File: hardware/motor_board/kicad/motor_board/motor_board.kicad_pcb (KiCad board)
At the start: 6 copper layers, 85 x 35 mm, 236 parts, among them J1 BOOMELE_1.27-2x10P, J2 WAFER-SH1.0-6PWB, J3 WAFER-SH1.0-6PWB, J4 S5B-XH-A, Q1 HYG015N04LS1C2, Q2 HYG015N04LS1C2, Q3 HYG015N04LS1C2, Q4 HYG015N04LS1C2, Q5 HYG015N04LS1C2, Q6 HYG015N04LS1C2, Q7 HYG015N04LS1C2, Q8 HYG015N04LS1C2, U1 STM32G474RET6, U10 SN74LVC3G17DCUR, U11 TPS22945DCKR, U12 TPS22945DCKR, U13 LM74502DDFR, U14 74LVC1G17SE-7, U2 DRV8323RHRGZR, U3 DRV8316CRRGFR, U4 DRV8316CRRGFR, U5 AP2112K-3.3TRG1, U6 SN74LVC08APWR, U7 INA239AIDGSR, U8 BQ76907RGRR, U9 SN74LVC3G17DCUR

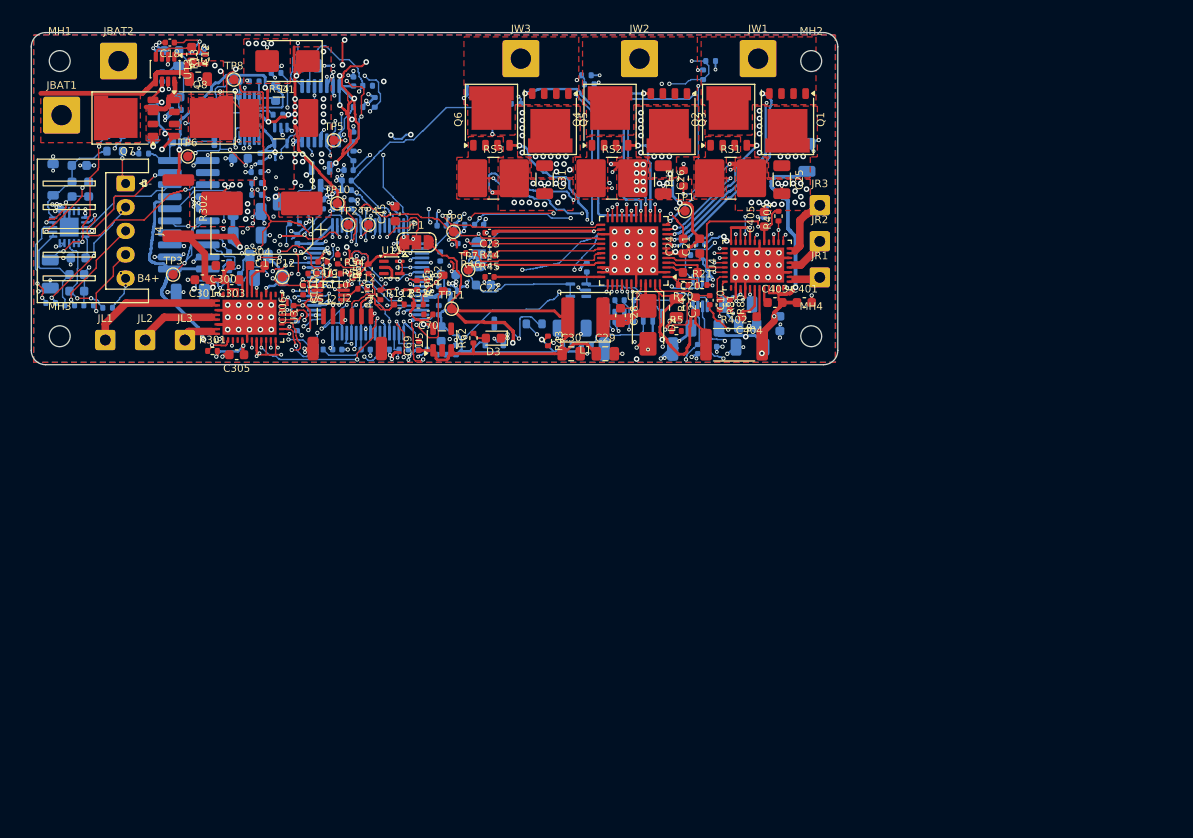
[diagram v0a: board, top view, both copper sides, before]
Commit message: v2: fresh 4-layer board built from the schematic (build_board.py): JLC041611-1080 stack-up, 85x35 outline, MH at the corners, all other parts staged off-board; design rules and custom DRC from JLC's 4-layer capabilities (with margin); 3D models applied. DRC 0, parity 0, 499 unrouted
Co-Authored-By: Claude Opus 5.5 (1M context) <noreply@anthropic.com>
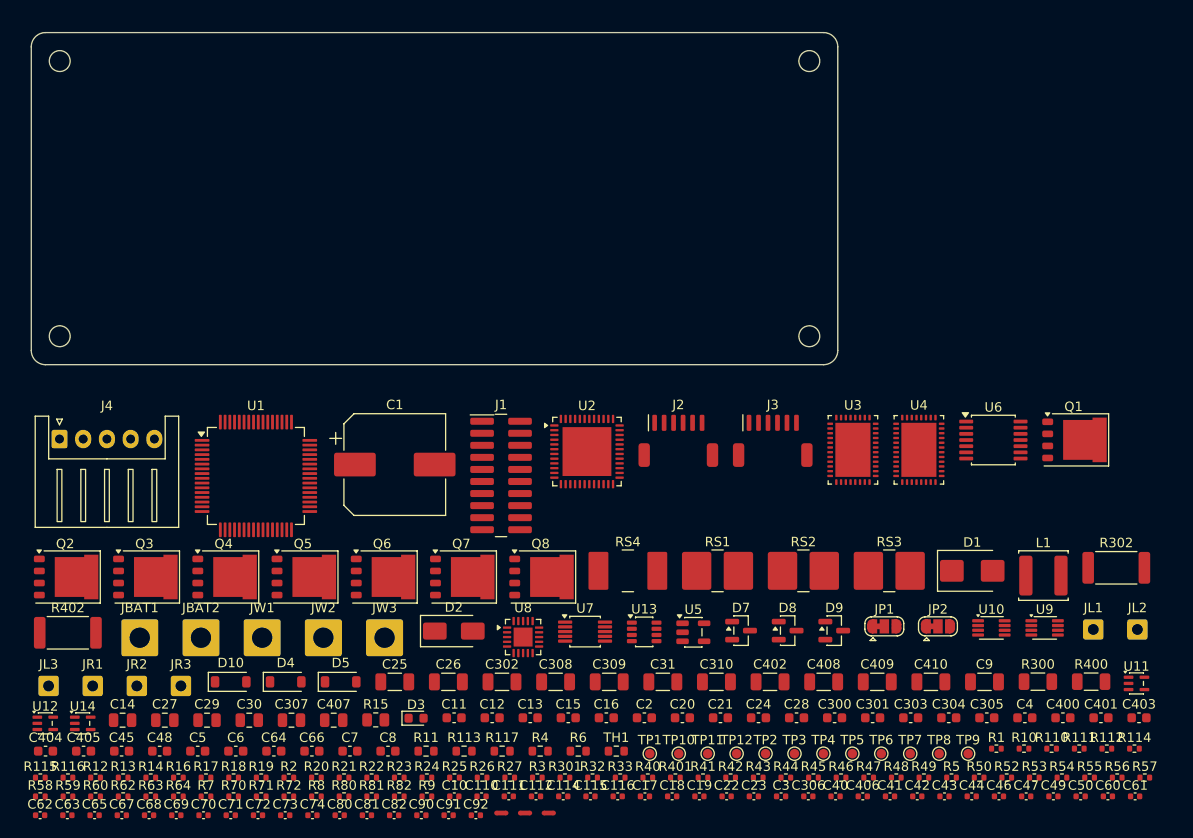
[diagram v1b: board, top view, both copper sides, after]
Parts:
- C11, C114, C115, C116, C13, C15, C16, C17, C19, C2, C3, C302, C307, C308, C309, C310, C4, C40, C400, C402, C406, C407, C408, C409, C41, C410, C42, C43, C44, C46, C48, C49, C5, C50, C6, C60, C61, C62, C63, C64, C65, C66, C67, C68, C7, C71, C73, C74, C8, C80, C81, C82, C9, C90, C91, D10, D4, D5, D7, D8, D9, J1, J3, JP2, R1, R10, R11, R114, R115, R116, R117, R12, R14, R15, R16, R17, R18, R19, R2, R22, R23, R24, R25, R26, R27, R3, R300, R32, R33, R40, R400, R41, R42, R47, R48, R49, R50, R53, R57, R58, R59, R6, R60, R63, R64, R7, R70, R71, R72, R8, R9, U1, U10, U12, U14, U6, U7, U8: moved to F.Cu
- moved C4 114.8 mm to (204.7, 142.2), turned to 0 degrees
- moved R1 112.9 mm to (201.7, 145.5), turned to 0 degrees
- moved JL2 108.9 mm to (216.6, 132.9)
- moved JL1 108.5 mm to (211.9, 132.9)
- moved C9 107.4 mm to (200.5, 138.4), turned to 0 degrees
- moved R10 107.2 mm to (204.6, 145.5), turned to 0 degrees
- moved R302 105.9 mm to (214.3, 126.4), turned to 0 degrees
- moved TP8 102.8 mm to (195.7, 146.0)
- moved R50 98.6 mm to (199.9, 148.5), turned to 0 degrees
- moved R56 97.3 mm to (214.4, 148.5), turned to 0 degrees
- moved TP6 96.5 mm to (189.6, 146.0)
- moved C18 95.5 mm to (167.5, 150.5), turned to 0 degrees
- moved C3 93.6 mm to (179.0, 150.5), turned to 0 degrees
- moved R49 93.6 mm to (194.1, 148.5)
- moved C47 93.1 mm to (204.9, 150.5), turned to 0 degrees
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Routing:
- net +3V3: track 349.5 -> 0.00 mm, vias 46 -> 0
- net GND: track 215.4 -> 0.00 mm, vias 269 -> 0
- net DRV_OFF: track 129.5 -> 0.00 mm, vias 5 -> 0
- net +5V: track 125.7 -> 0.00 mm, vias 2 -> 0
- net VBAT: track 116.9 -> 0.00 mm, vias 58 -> 0
- net SPI_SCK: track 101.7 -> 0.00 mm, vias 6 -> 0
- net W_EN: track 91.9 -> 0.00 mm, vias 7 -> 0
- net SPI_MISO: track 85.3 -> 0.00 mm, vias 6 -> 0
- net SPI_MOSI: track 79.7 -> 0.00 mm, vias 5 -> 0
- net W_VA: track 73.6 -> 0.00 mm, vias 7 -> 0
- net W_NTC: track 72.8 -> 0.00 mm, vias 7 -> 0
- net W_INLB_M: track 69.7 -> 0.00 mm, vias 7 -> 0
- net R_nFAULT: track 67.9 -> 0.00 mm, vias 2 -> 0
- net W_SOC: track 66.6 -> 0.00 mm, vias 10 -> 0
- net W_nFAULT: track 66.3 -> 0.00 mm, vias 8 -> 0
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- removed copper zone on In3.Cu, net +3V3
- removed copper zone on F.Cu, net /power/BAT_IN
- removed copper zone on F.Cu, net /power/PSW_S
- removed copper zone on F.Cu, net /power/VBAT_SW
- removed copper zone on F.Cu, net /weapon/W_A
- removed copper zone on F.Cu, net /weapon/W_B
- removed copper zone on F.Cu, net /weapon/W_C
- removed copper zone on F.Cu, net /weapon/W_SLA
- removed copper zone on F.Cu, net /weapon/W_SLB
- removed copper zone on F.Cu, net /weapon/W_SLC
- removed copper zone on B.Cu, net GND
- removed copper zone on F.Cu, net GND
- removed copper zone on In1.Cu, net GND
- removed copper zone on In4.Cu, net GND
- removed copper zone on F.Cu, net VBAT
- removed copper zone on In2.Cu, net VBAT
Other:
- copper layers 6 -> 4
- board text removed: "B-"
- board text removed: "B4+"
- board text removed: "BAT+"
- board text removed: "BAT-"
- board text removed: "FRONT (drum)"
- board text removed: "LA"
- board text removed: "LB"
- board text removed: "LC"
- board text removed: "MOTOR BOARD rev L"
- board text removed: "RA"
- board text removed: "RB"
- board text removed: "RC"
- board text removed: "T"
- board text removed: "VS J2"
- board text removed: "VS J3"
- board text removed: "WA"
- board text removed: "WB"
- board text removed: "WC"

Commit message: v2 package swaps (rev L2), after adversarial review: U6 WQFN-14 (EP to GND), D2 PMEG4030ER, L1 ZEMS404030 4.1 mm, J4 vertical XH, J2/J3 genuine JST vertical SH, R300/R400 0603 anti-surge, R15/C14/D10 one size down; drive VM bulk 2 x 10 uF X7R 1210 per drive (C309/C310/C409/C410 removed, user OK) - the 1206 X5R kept only ~2.3 uF at 16.8 V
sim_hotplug.py models MLCC DC bias (worst bounce 2.14 V/us at 0 C, 2.62 at -40 C); library check 0 errors, mutation test all caught; schematic regenerated, nets 176/176; v2 board rebuilt: DRC 0, parity 0; WQFN-14 3D model generated; DESIGN/calcs/BOM/FAB/CHANGES updated (CPL rotation fix for J2/J3/J4)

Co-Authored-By: Claude Opus 5.5 (1M context) <noreply@anthropic.com>
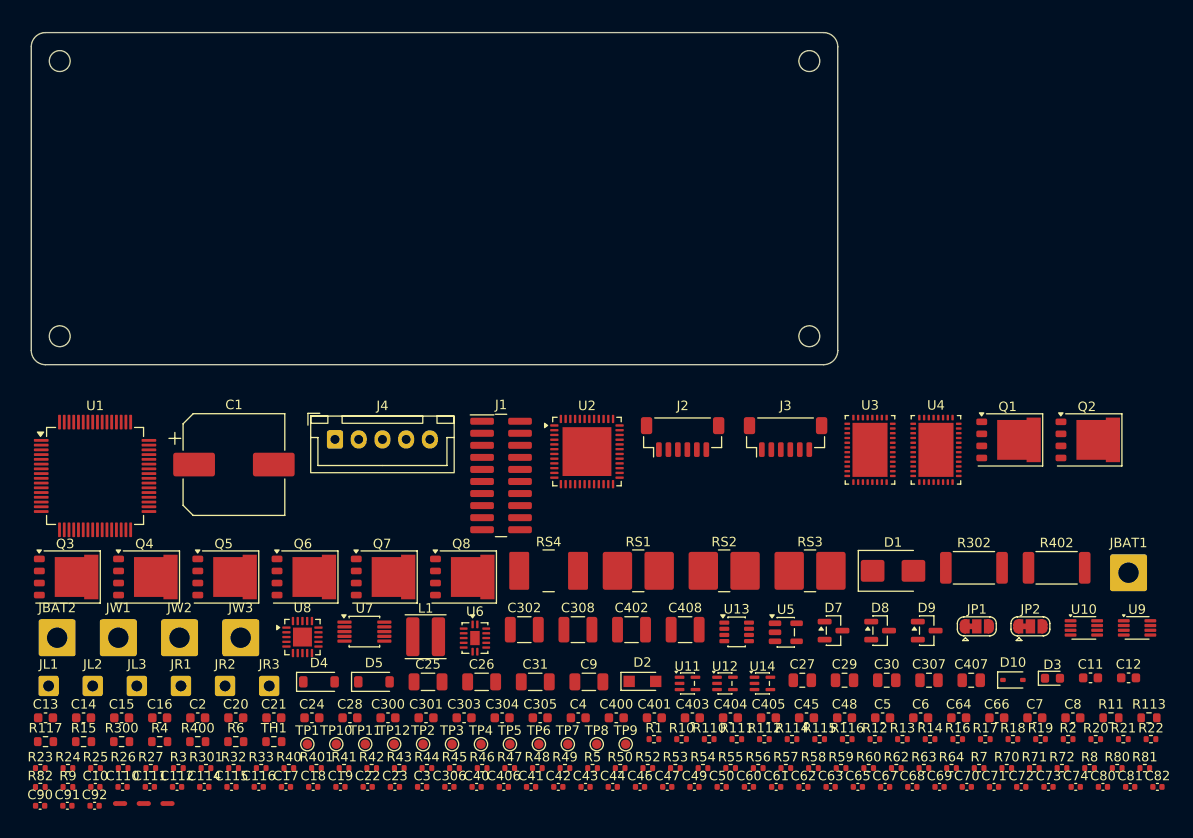
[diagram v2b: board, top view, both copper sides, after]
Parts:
- removed C309, C310, C409, C410: 10uF 50V, Capacitor_SMD:C_1206_3216Metric
- C14: footprint Capacitor_SMD:C_0805_2012Metric -> Capacitor_SMD:C_0603_1608Metric
- C302, C308, C402, C408: value 10uF 50V -> 10uF 50V X7R 1210; footprint Capacitor_SMD:C_1206_3216Metric -> Capacitor_SMD:C_1210_3225Metric
- D10: value 1N4148W -> 1N4148WS; footprint Diode_SMD:D_SOD-123 -> Diode_SMD:D_SOD-323
- D2: value SS34 -> PMEG4030ER; footprint Diode_SMD:D_SMA -> Diode_SMD:Nexperia_CFP3_SOD-123W
- J2, J3: value WAFER-SH1.0-6PWB -> BM06B-SRSS-TB; footprint motor_board:SH1.0-6P_RA_XUNPU_WAFER-SH1.0-6PWB -> Connector_JST:JST_SH_BM06B-SRSS-TB_1x06-1MP_P1.00mm_Vertical
- J4: value S5B-XH-A -> B5B-XH-A; footprint Connector_JST:JST_XH_S5B-XH-A_1x05_P2.50mm_Horizontal -> Connector_JST:JST_XH_B5B-XH-A_1x05_P2.50mm_Vertical
- L1: value FNR5040S220MT -> ZEMS404030-220M; footprint Inductor_SMD:L_Changjiang_FNR5040S -> Inductor_SMD:L_Changjiang_FTC404030S
- R15: value 6.8k 0805 -> 6.8k 0603; footprint Resistor_SMD:R_0805_2012Metric -> Resistor_SMD:R_0603_1608Metric
- R300, R400: value 22R 1206 -> 22R 0603 anti-surge; footprint Resistor_SMD:R_1206_3216Metric -> Resistor_SMD:R_0603_1608Metric
- U6: value SN74LVC08APWR -> SN74LVC08ABQAR; footprint Package_SO:TSSOP-14_4.4x5mm_P0.65mm -> Package_DFN_QFN:DHWQFN-14-1EP_2.5x3mm_P0.5mm_EP1x1.5mm
- moved JL1 110.3 mm to (101.8, 138.9)
- moved JL2 110.3 mm to (106.5, 138.9)
- moved Q2 108.6 mm to (211.2, 112.9)
- moved R402 104.4 mm to (208.1, 126.4)
- moved JBAT1 104.4 mm to (215.6, 126.9)
- moved R300 96.8 mm to (109.5, 144.7)
- moved R400 94.4 mm to (117.5, 144.7)
- moved D10 82.4 mm to (203.5, 138.2)
- moved R17 82.2 mm to (200.5, 144.5)
- moved R115 82.2 mm to (183.1, 144.5)
- moved R116 82.2 mm to (186.0, 144.5)
- moved R19 82.2 mm to (206.4, 144.5)
- moved R2 82.2 mm to (209.3, 144.5)
- moved R12 82.2 mm to (188.9, 144.5)
- moved R13 82.2 mm to (191.8, 144.5)
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
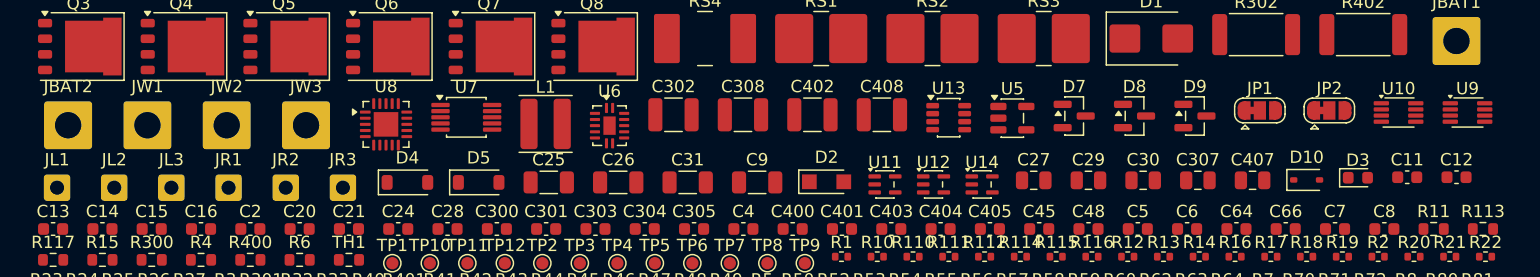
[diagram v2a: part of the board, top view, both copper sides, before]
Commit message: C25/C26/C31 -> 10 uF 50 V X7R 1210 (C77102, user OK): VDS-only fault kick at the DRV8316 VM 7.7 -> 4.3 V/us, bus peak ~30 -> ~22 V; hot-plug worst 1.86 V/us (0 C), 2.14 (-40 C), re-close 1.77; schematic regenerated (nets 176/176), board rebuilt (DRC 0, parity 0); DESIGN/calcs/BOM/CHANGES updated
Co-Authored-By: Claude Opus 5.5 (1M context) <noreply@anthropic.com>
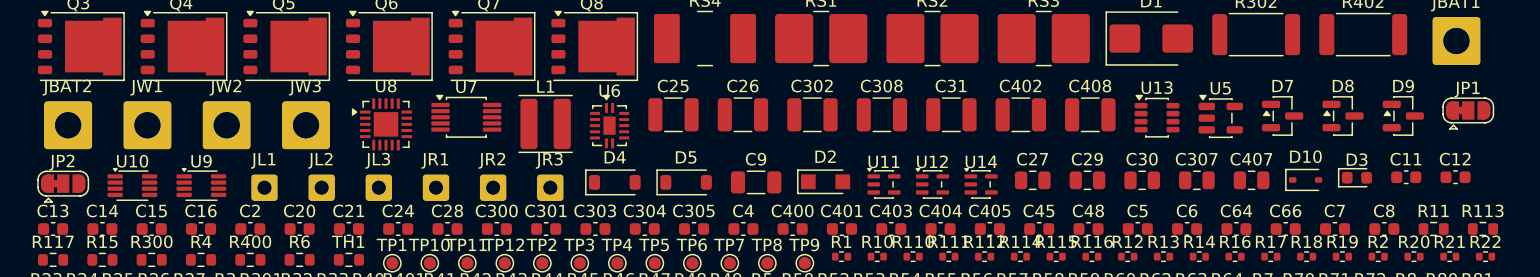
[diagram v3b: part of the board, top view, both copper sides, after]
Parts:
- C25, C26, C31: value 10uF 50V -> 10uF 50V X7R 1210; footprint Capacitor_SMD:C_1206_3216Metric -> Capacitor_SMD:C_1210_3225Metric
- moved JP2 103.1 mm to (102.3, 138.5)
- moved U10 103.1 mm to (108.0, 138.7)
- moved U9 103.1 mm to (113.6, 138.7)
- moved C31 22.1 mm to (174.6, 132.9)
- moved D8 17.0 mm to (206.4, 133.0)
- moved JP1 17.0 mm to (216.6, 132.6)
- moved U5 17.0 mm to (196.5, 133.2)
- moved C402 17.0 mm to (180.2, 132.9)
- moved C408 17.0 mm to (185.9, 132.9)
- moved D7 16.9 mm to (201.5, 133.0)
- moved D9 16.9 mm to (211.3, 133.0)
- moved U13 16.9 mm to (191.3, 133.2)
- moved D4 16.9 mm to (147.2, 138.4)
- moved D5 16.9 mm to (153.0, 138.4)
- moved JL2 16.9 mm to (123.3, 138.9)
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
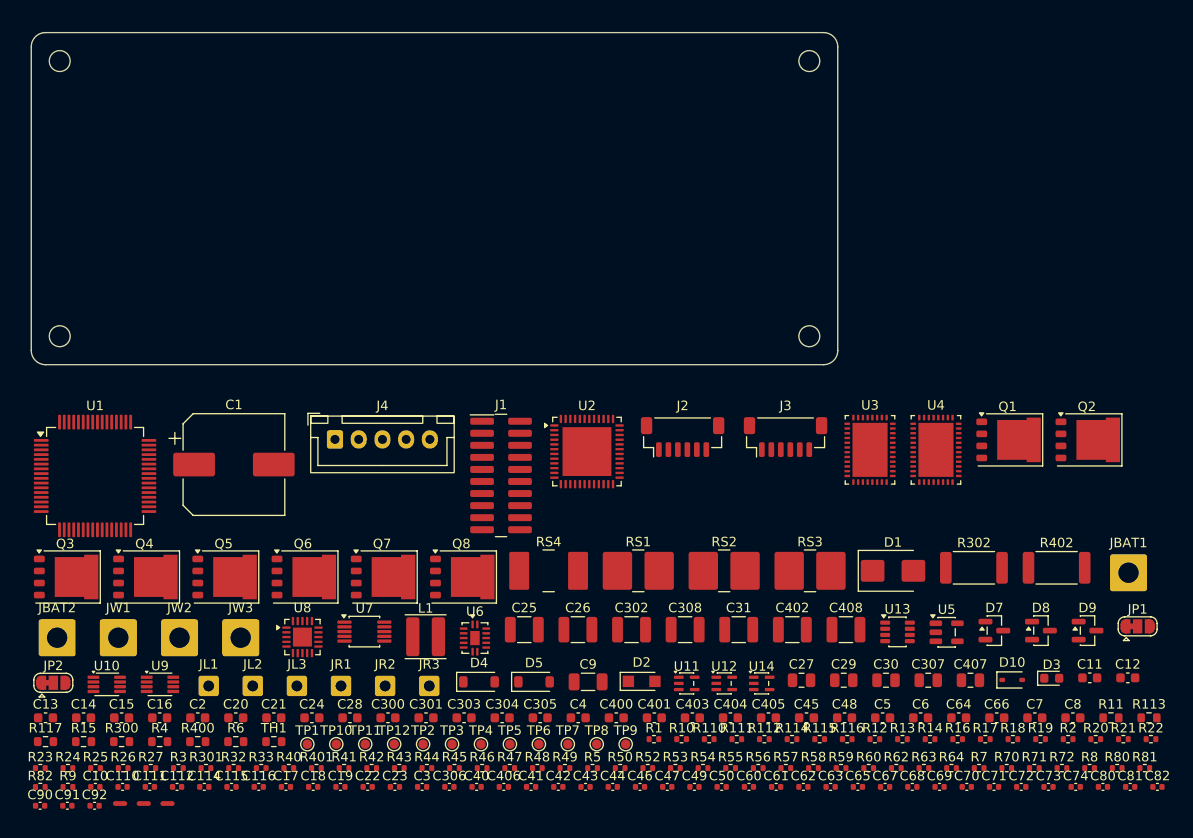
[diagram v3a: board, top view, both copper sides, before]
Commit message: v2 P1 placement: kicad/v2/place.py (attempt-1 engine + block regions) and spec.py (explicit key parts per the approved floorplan, the rest anchored automatically to the IC pin/net they serve); render.py; no courtyard overlaps (DRC: silk only), top 67 %, bottom 19 %
Co-Authored-By: Claude Opus 5.5 (1M context) <noreply@anthropic.com>
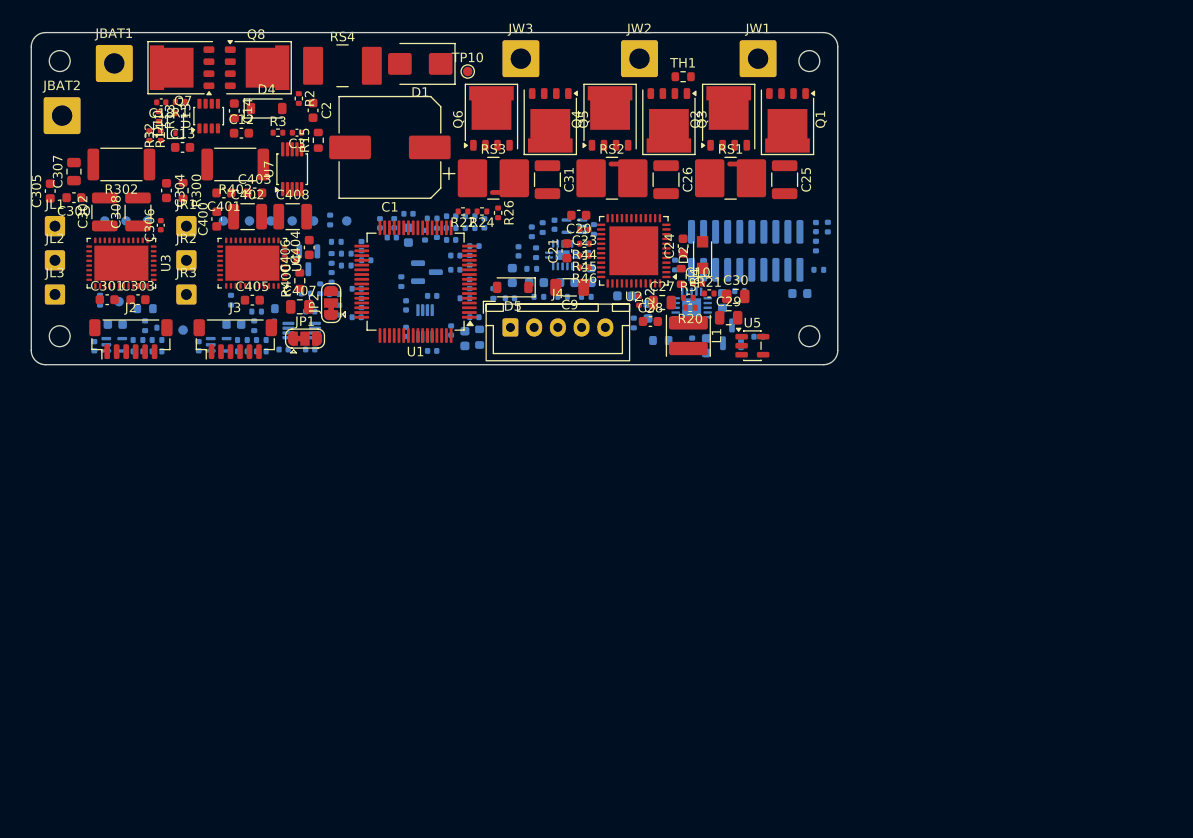
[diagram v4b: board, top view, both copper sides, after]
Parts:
- C11, C110, C111, C112, C114, C115, C116, C15, C16, C17, C19, C4, C40, C41, C42, C43, C44, C45, C46, C47, C48, C49, C5, C50, C6, C60, C61, C62, C63, C64, C65, C66, C67, C68, C69, C7, C70, C71, C72, C73, C74, C8, C80, C81, C82, C90, C91, C92, D3, D7, D8, D9, J1, R10, R11, R110, R111, R112, R113, R114, R115, R116, R117, R12, R16, R17, R18, R19, R23, R25, R27, R301, R33, R40, R401, R41, R42, R43, R47, R48, R49, R50, R52, R53, R54, R55, R56, R57, R58, R59, R6, R60, R62, R63, R64, R7, R70, R71, R72, R8, R80, R81, R82, R9, TP1, TP11, TP12, TP2, TP3, TP4, TP5, TP6, TP7, TP8, TP9, U10, U11, U12, U14, U6, U8, U9: moved to B.Cu
- moved JBAT1 119.6 mm to (108.8, 73.2)
- moved R113 114.2 mm to (112.0, 99.1), turned to 180 degrees
- moved C12 109.6 mm to (122.2, 80.6)
- moved D10 105.9 mm to (115.2, 79.5), turned to 90 degrees
- moved R2 105.5 mm to (128.2, 77.0), turned to -90 degrees
- moved C307 104.8 mm to (104.5, 84.7), turned to 90 degrees
- moved R14 104.0 mm to (112.5, 80.8), turned to -90 degrees
- moved R13 102.2 mm to (113.5, 78.8), turned to -90 degrees
- moved R81 99.4 mm to (133.2, 94.5)
- moved R302 99.4 mm to (109.5, 83.9), turned to 180 degrees
- moved R80 97.7 mm to (133.2, 93.3)
- moved R402 96.4 mm to (121.5, 83.9), turned to 180 degrees
- moved C81 95.7 mm to (134.8, 98.5), turned to -90 degrees
- moved C80 94.6 mm to (134.3, 97.0), turned to 180 degrees
- moved R72 94.5 mm to (132.2, 92.0)
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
